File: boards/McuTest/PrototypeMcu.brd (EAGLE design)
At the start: 50.8 x 25.4 mm, 30 parts, among them IC1 REG1118, J1 10118193-0001LF, Q1 8MHz, SW1 B3U-1000P-2P-SMD

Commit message: Design rules check out
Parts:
- moved C12 1.27 mm to (10.4, 18.8)
- moved JP4 0.57 mm to (48.3, 13.2)
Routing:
- net GPIO0: track 0.00 -> 18.7 mm, vias 0 -> 1
- net GND: track 0.02 -> 5.82 mm, vias 0 -> 27
- net N$2: track 11.4 -> 15.6 mm
- net N$5: track 10.2 -> 12.5 mm
- net GPIO5: track 19.4 -> 20.5 mm
- net OSC32_OUT: track 9.29 -> 9.90 mm
- added copper zone on layer 1, net GND
- added copper zone on layer 16, net GND

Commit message: DRC changes
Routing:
- net GND: track 5.82 -> 10.4 mm
- net OSC32_OUT: track 9.90 -> 9.26 mm
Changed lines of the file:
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@@
 <contactref element="CR1" pad="3"/>
 <wire x1="18.288" y1="20.686" x2="18.288" y2="18.542" width="0.254" layer="1"/>
-<wire x1="18.288" y1="17.43446875" x2="20.401234375" y2="15.321234375" width="0.254" layer="1"/>
-<wire x1="18.288" y1="17.43446875" x2="18.288" y2="18.542" width="0.254" layer="1"/>
-<wire x1="20.401234375" y1="15.321234375" x2="20.44556875" y2="15.2769" width="0.254" layer="1"/>
+<wire x1="18.288" y1="18.542" x2="18.288" y2="17.43446875" width="0.254" layer="1"/>
 <wire x1="20.44556875" y1="15.2769" x2="21.217" y2="15.2769" width="0.254" layer="1"/>
 <wire x1="21.217" y1="15.2769" x2="21.2979" y2="15.196" width="0.254" layer="1"/>
+<wire x1="18.288" y1="17.43446875" x2="20.44556875" y2="15.2769" width="0.254" layer="1"/>
 </signal>
 <signal name="OSC32_OUT">
@@
 <contactref element="C2" pad="1"/>
 <contactref element="CR1" pad="4"/>
-<wire x1="21.217" y1="14.7769" x2="20.574" y2="14.7769" width="0.254" layer="1"/>
 <wire x1="20.574" y1="14.7769" x2="20.19156875" y2="14.7769" width="0.254" layer="1"/>
 <wire x1="17.44246875" y1="17.526" x2="16.764" y2="17.526" width="0.254" layer="1"/>
@@
 <vertex x="50.8" y="25.4"/>
 </polygon>
-<wire x1="30.174" y1="6.8199" x2="30.1867" y2="6.8072" width="0.254" layer="1"/>
-<wire x1="30.48" y1="5.74246875" x2="30.48" y2="5.588" width="0.254" layer="1"/>
-<wire x1="30.1867" y1="6.8072" x2="30.1867" y2="6.03576875" width="0.254" layer="1"/>
-<wire x1="30.1867" y1="6.03576875" x2="30.48" y2="5.74246875" width="0.254" layer="1"/>
 <via x="22.86" y="8.382" extent="1-16" drill="0.35"/>
 <wire x1="23.5931" y1="7.67223125" x2="23.5931" y2="7.3949" width="0.254" layer="1"/>
@@
 <via x="12.446" y="10.16" extent="1-16" drill="0.35"/>
 <via x="19.812" y="20.828" extent="1-16" drill="0.35"/>
+<wire x1="30.174" y1="6.8199" x2="30.2121" y2="6.7818" width="0.2032" layer="1"/>
+<wire x1="32.940871875" y1="5.497025" x2="33.3930125" y2="5.044884375" width="0.2032" layer="1"/>
+<wire x1="33.3930125" y1="5.044884375" x2="33.934328125" y2="5.044884375" width="0.2032" layer="1"/>
+<wire x1="33.934328125" y1="5.044884375" x2="34.1874125" y2="5.29796875" width="0.2032" layer="1"/>
+<wire x1="34.1874125" y1="5.29796875" x2="34.87170625" y2="5.29796875" width="0.2032" layer="1"/>
+<wire x1="30.2121" y1="6.7818" x2="30.2121" y2="6.0462875" width="0.2032" layer="1"/>
+<wire x1="30.2121" y1="6.0462875" x2="30.7613625" y2="5.497025" width="0.2032" layer="1"/>
+<wire x1="30.7613625" y1="5.497025" x2="32.940871875" y2="5.497025" width="0.2032" layer="1"/>
 </signal>
 <signal name="OSC8_IN">
@@
 <contactref element="R2" pad="2"/>
 <contactref element="CR1" pad="6"/>
-<wire x1="18.034" y1="14.724" x2="18.990475" y2="14.724" width="0.254" layer="1"/>
-<wire x1="18.990475" y1="14.724" x2="19.9052375" y2="13.8092375" width="0.254" layer="1"/>
-<wire x1="19.9052375" y1="13.8092375" x2="19.937575" y2="13.7769" width="0.254" layer="1"/>
-<wire x1="19.9052375" y1="13.8092375" x2="21.2979" y2="13.696" width="0.254" layer="1"/>
+<wire x1="18.034" y1="14.724" x2="19.09499375" y2="14.724" width="0.254" layer="1"/>
+<wire x1="21.217" y1="13.7769" x2="21.2979" y2="13.696" width="0.254" layer="1"/>
+<wire x1="19.09499375" y1="14.724" x2="20.04209375" y2="13.7769" width="0.254" layer="1"/>
+<wire x1="20.04209375" y1="13.7769" x2="21.217" y2="13.7769" width="0.254" layer="1"/>
 </signal>
 <signal name="N_RST">
@@
 <contactref element="CR1" pad="29"/>
 <contactref element="S3" pad="2"/>
-<wire x1="29.174" y1="6.8199" x2="29.21" y2="3.556" width="0.2032" layer="1"/>
+<wire x1="29.174" y1="6.8199" x2="29.21" y2="6.7839" width="0.1524" layer="1"/>
+<wire x1="29.21" y1="6.7839" x2="29.21" y2="3.556" width="0.1524" layer="1"/>
 </signal>
 <signal name="USART3_RX">
 <contactref element="CR1" pad="30"/>
 <contactref element="S3" pad="1"/>
-<wire x1="29.674" y1="6.8199" x2="29.7549" y2="6.739" width="0.254" layer="1"/>
-<wire x1="29.7549" y1="6.739" x2="29.7549" y2="5.45956875" width="0.254" layer="1"/>
-<wire x1="29.7549" y1="5.45956875" x2="31.75" y2="3.556" width="0.2032" layer="1"/>
+<wire x1="29.674" y1="6.8199" x2="29.8057" y2="6.6882" width="0.1524" layer="1"/>
+<wire x1="31.75" y1="3.7874125" x2="31.75" y2="3.556" width="0.1524" layer="1"/>
+<wire x1="29.8057" y1="6.6882" x2="29.8057" y2="5.7317125" width="0.1524" layer="1"/>
+<wire x1="29.8057" y1="5.7317125" x2="31.75" y2="3.7874125" width="0.1524" layer="1"/>
 </signal>
 <signal name="USART1_TX">

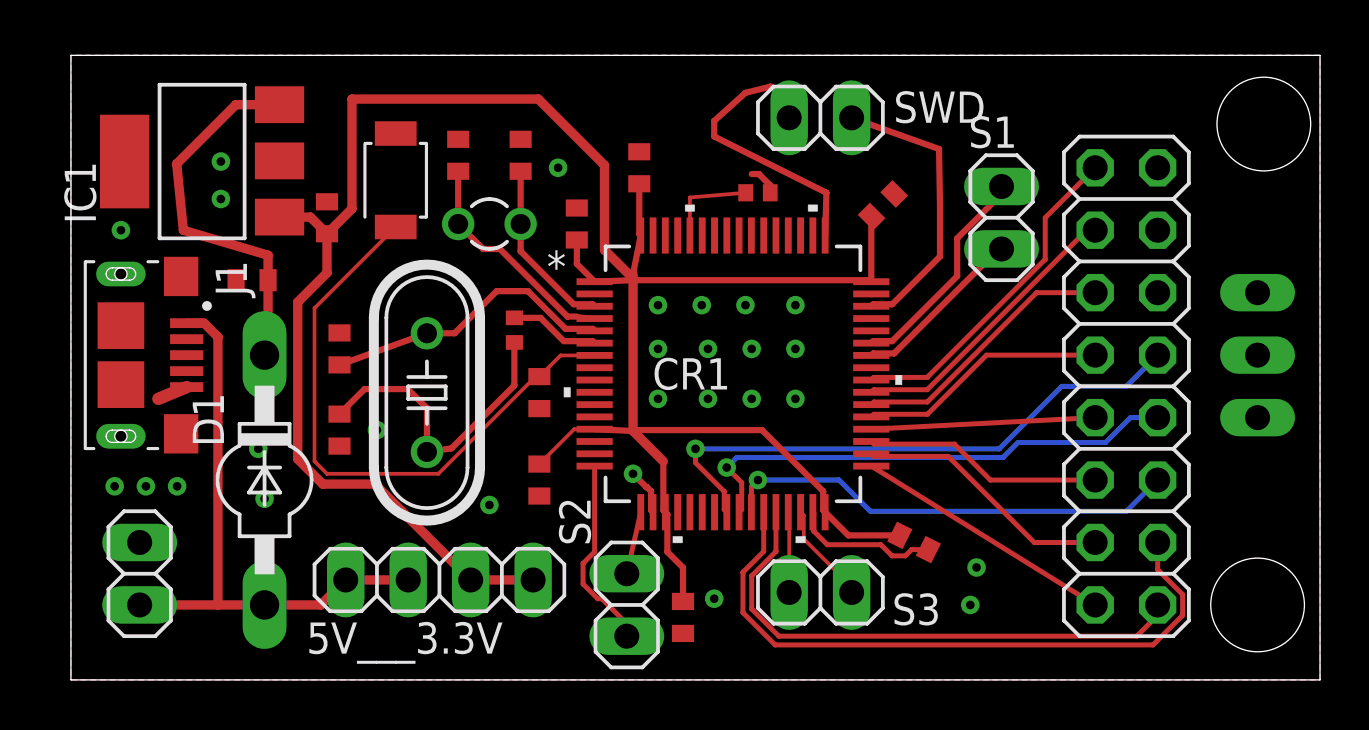
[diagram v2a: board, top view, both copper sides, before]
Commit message: Added a fuse and impedance matched clock signals
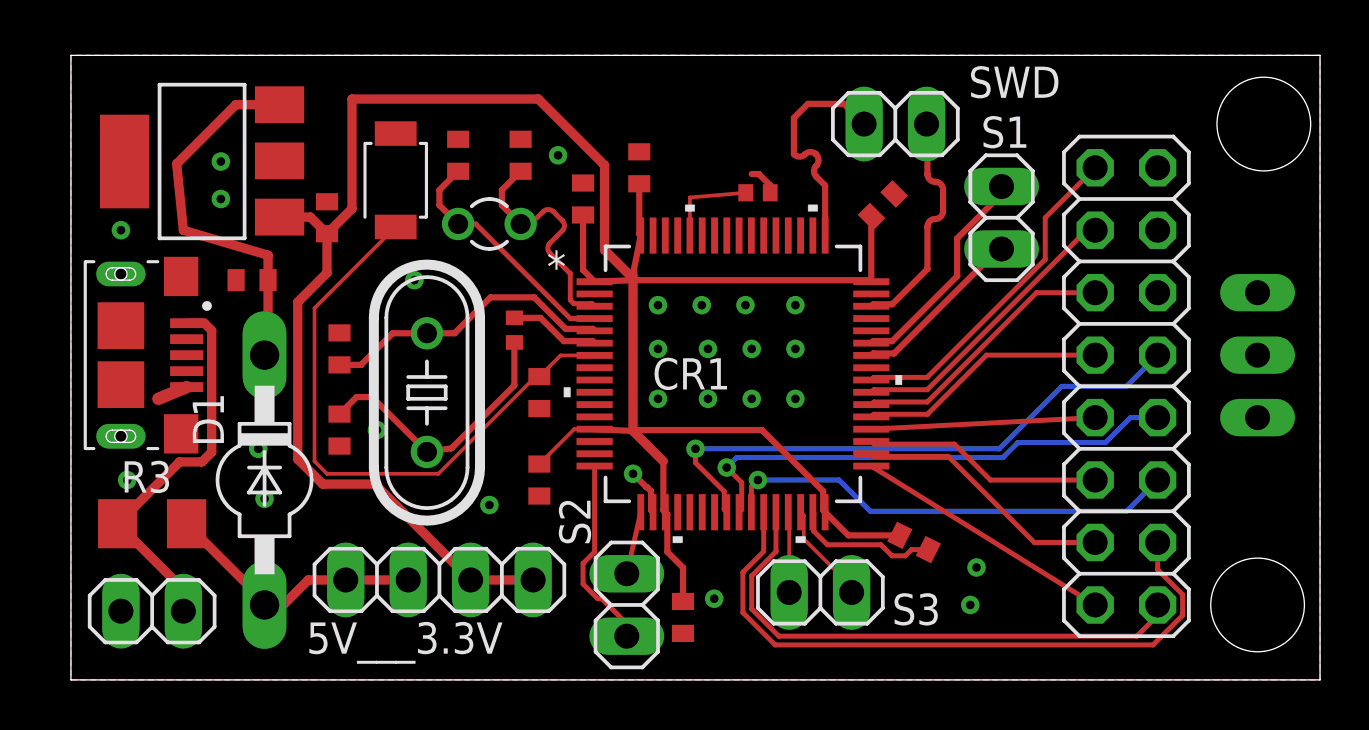
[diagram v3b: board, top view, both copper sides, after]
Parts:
- added R3: (no value), rcl:M1206
- moved SWD 3.06 mm to (33.5, 22.6)
- moved JP1 1.61 mm to (3.30, 2.79), turned to 0 degrees
- moved C6 1.05 mm to (20.8, 19.6)
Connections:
- new net N$16: J1.1, JP1.2, R3.1
- net N$4: now also R3.2; no longer J1.1, JP1.2
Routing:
- net N$16: track 0.00 -> 15.8 mm
- net N$4: track 23.7 -> 10.9 mm
- net N$8: track 11.9 -> 9.27 mm
- net OSC32_IN: track 7.19 -> 9.70 mm
- net N$6: track 11.8 -> 9.35 mm
- net N$5: track 12.5 -> 11.1 mm
- net VDD: track 97.3 -> 98.2 mm
- net OSC32_OUT: track 9.26 -> 9.92 mm
- net GND: vias 27 -> 26

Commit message: LED and silkscreen Aded
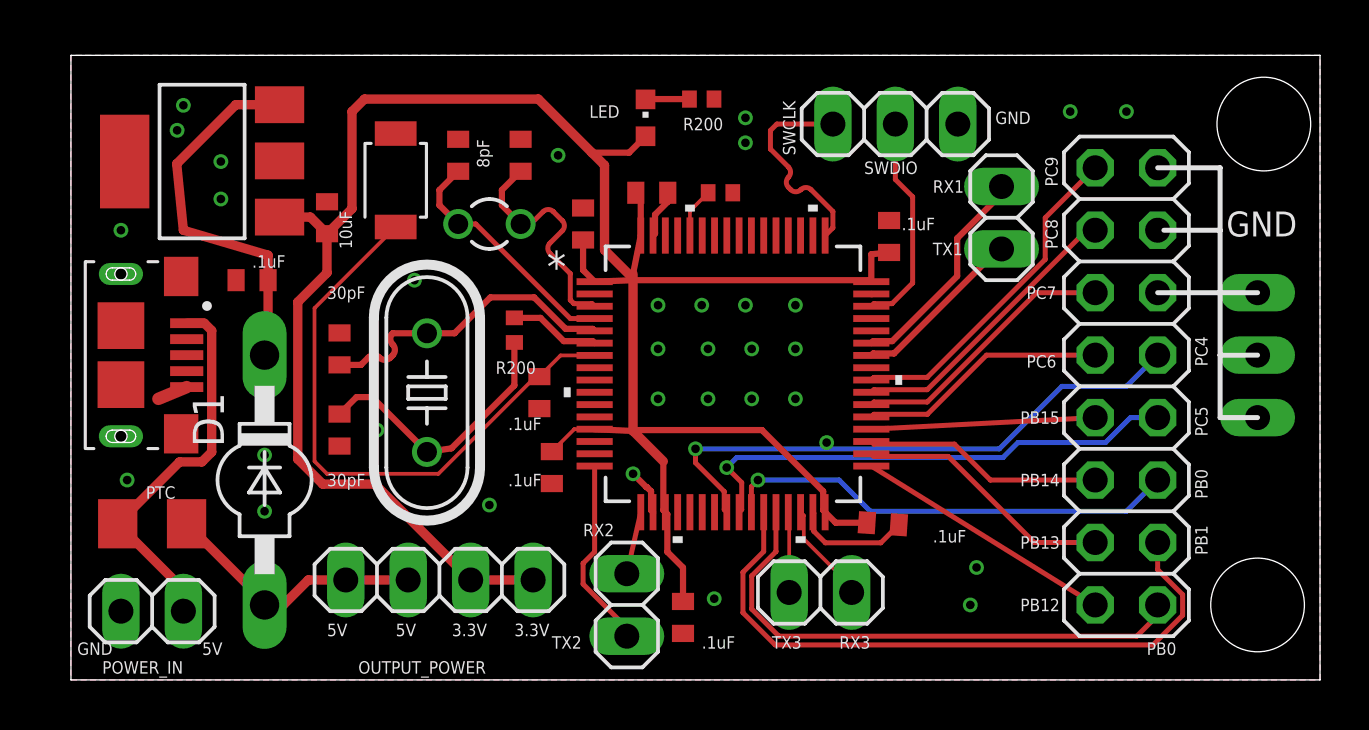
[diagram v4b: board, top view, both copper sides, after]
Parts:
- added LED1: (no value), led:CHIPLED_0603
- added R4: 200, rcl:R0402
- SWD: device pinhead:1X02 -> pinhead:1X03
- moved R1 1.52 mm to (26.4, 19.8)
- moved C11 1.48 mm to (33.0, 6.35), turned to 356.2 degrees
- moved C8 1.30 mm to (33.3, 18.0), turned to 90 degrees
- moved C7 1.14 mm to (23.6, 19.8), turned to 0 degrees
- moved C6 1.02 mm to (20.8, 18.5)
- moved C9 0.72 mm to (19.6, 8.64)
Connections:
- new net N$15: LED1.C, R4.1
- net GND: now also R4.2, SWD.3
- net VDD: now also LED1.A
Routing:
- net VDD: track 98.2 -> 96.0 mm
- net N$15: track 0.00 -> 1.79 mm
- net N$1: track 3.82 -> 2.05 mm
- net N$8: track 9.27 -> 8.59 mm
- net OSC8_IN: track 12.1 -> 12.6 mm
- net N$6: track 9.35 -> 8.83 mm
- net GND: track 10.4 -> 9.96 mm, vias 26 -> 33
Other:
- board text added: ".1uF"
- board text added: "10uF"
- board text added: "3.3V"
- board text added: "30pF"
- board text added: "5V"
- board text added: "8pF"
- board text added: "GND"
- board text added: "LED"
- board text added: "OUTPUT_POWER"
- board text added: "PB0"
- board text added: "PB1"
- board text added: "PB12"
- board text added: "PB13"
- board text added: "PB14"
- board text added: "PB15"
- board text added: "PC4"
- board text added: "PC5"
- board text added: "PC6"
- board text added: "PC7"
- board text added: "PC8"
- board text added: "PC9"
- board text added: "POWER_IN"
- board text added: "PTC"
- board text added: "R200"
- board text added: "RX1"
- board text added: "RX2"
- board text added: "RX3"
- board text added: "SWCLK"
- board text added: "SWDIO"
- board text added: "TX1"
- board text added: "TX2"
- board text added: "TX3"

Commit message: Order placed to OSH Park
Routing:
- net VDD: track 96.0 -> 98.0 mm
- net GPIO4: track 23.5 -> 22.2 mm
- net N$2: track 15.6 -> 14.6 mm
- net N$14: track 10.7 -> 11.4 mm
- net GPIO5: track 20.5 -> 19.8 mm
- net N$5: track 11.1 -> 10.6 mm
- net OSC8_IN: track 12.6 -> 12.1 mm
- net GND: vias 33 -> 35
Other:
- board text added: "Keith Aylwin"
- board text added: "V1"
